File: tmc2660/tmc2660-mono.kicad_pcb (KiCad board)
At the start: 4 copper layers, 25 x 40 mm, 19 parts, among them J1 0R, P3 Motor, U1 TMC2660

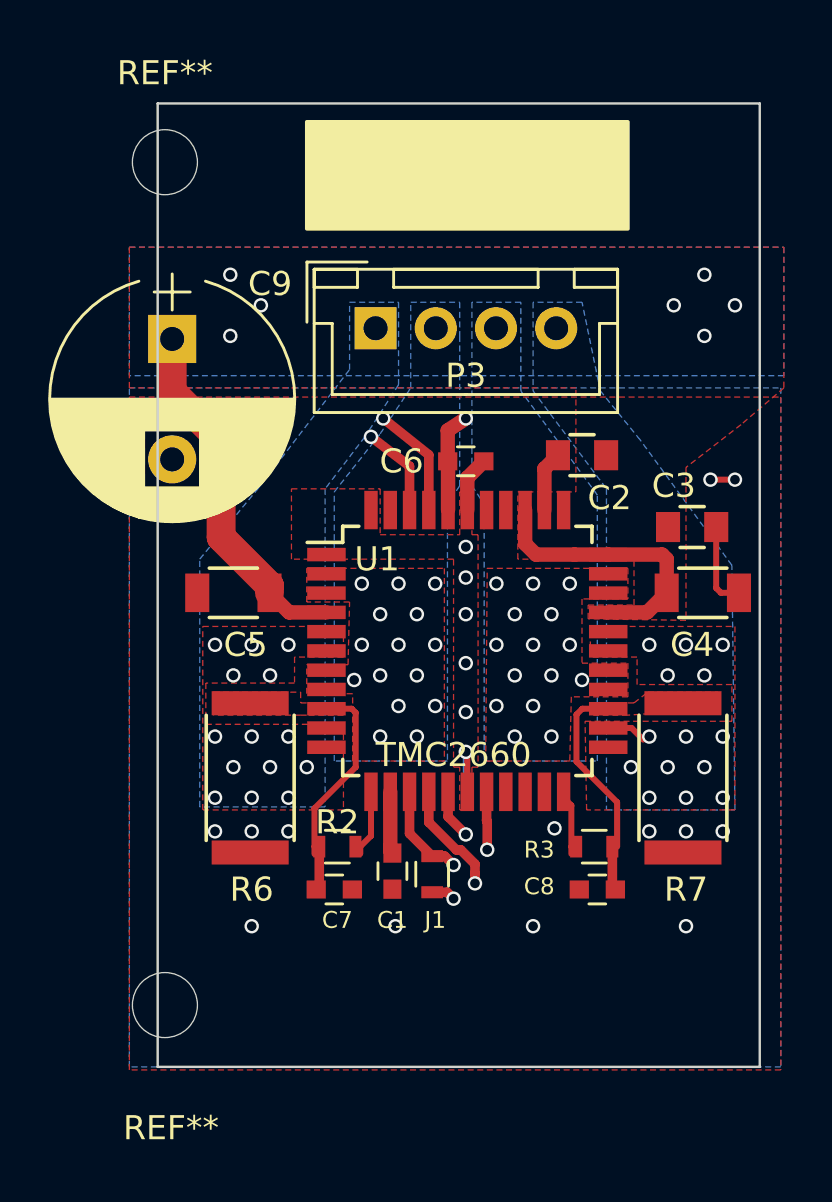
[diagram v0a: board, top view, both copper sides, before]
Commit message: Adapt some vias around the SPI connect to fix a gap in the TopCu copper pour.
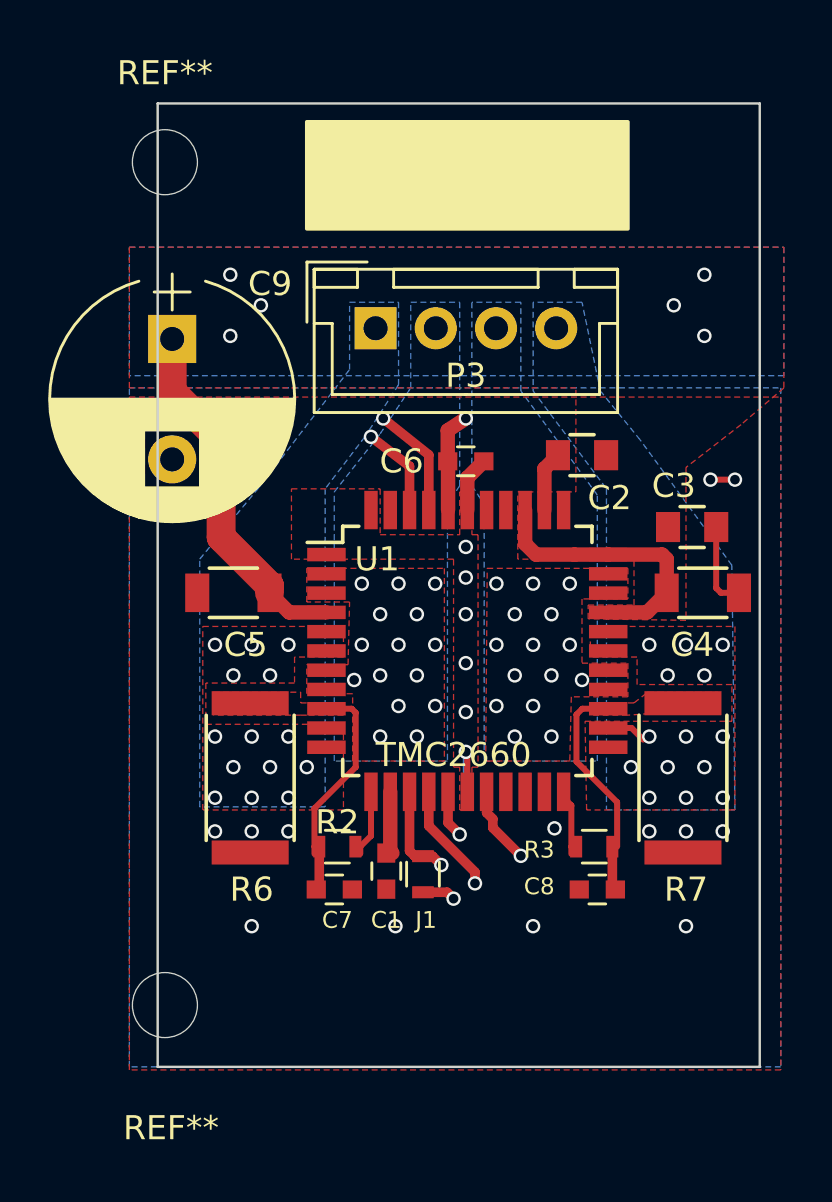
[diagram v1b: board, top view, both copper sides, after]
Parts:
- moved J1 0.38 mm to (128.0, 63.6)
- moved C1 0.25 mm to (126.5, 63.5)
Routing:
- net /CS_1: track 30.5 -> 31.7 mm
- net VMot: vias 7 -> 6
